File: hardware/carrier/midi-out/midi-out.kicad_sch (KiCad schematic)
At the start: 7 parts

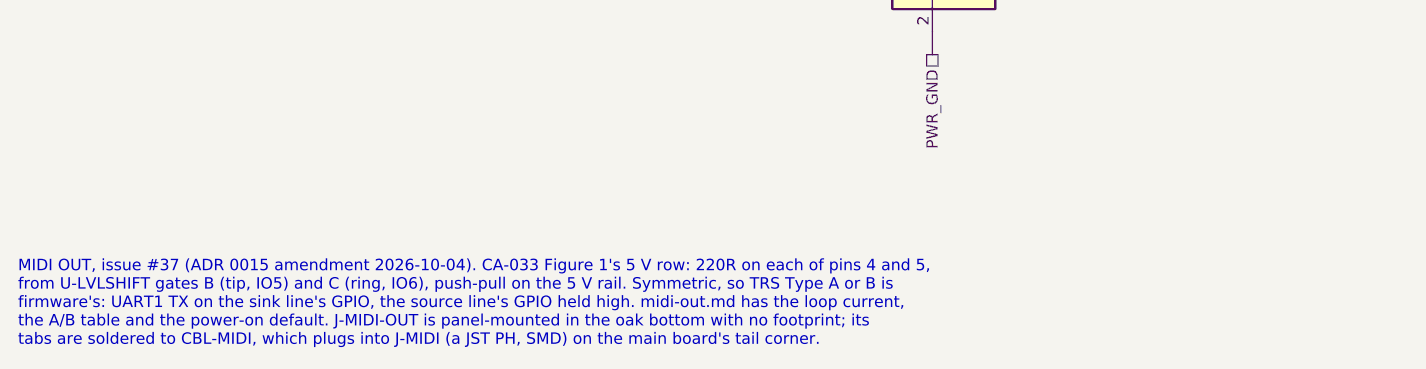
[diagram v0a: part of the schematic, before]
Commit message: #37: midi-out sheet text named the old GPIOs; carrier sheet renders re-ledgered
The midi-out sheet's note said gates B (tip, IO5) and C (ring, IO6).
It is IO6 and IO2 since the ribbon re-pin. Fixed and re-rendered. The
carrier, led-strip-drive, breath-adc and power-entry-instrument renders came
out identical and are re-ledgered in hardware/SHEETS.csv.

Gate-Red: pre-existing main-board/module-main kicad failures; boards/module-iso has no coverage row (arrived with integration bcd1f0c); interfaces/system sim stale; body renders and photos deferred to one rebuild after #36/#37 merge (coordinator); DXFs and clash pending (one heavy job at a time); main-board.kicad_pcb parity on IO2/IO6 and U-LVLSHIFT pins 5/6/8/9, R48/R49 and the MIDI parts unplaced (#35 has the board)

Co-Authored-By: Claude Opus 5.5 <noreply@anthropic.com>
Claude-Session: https://claude.ai/code/session_01LmB4muFXnoLprWX4JzuJ5A
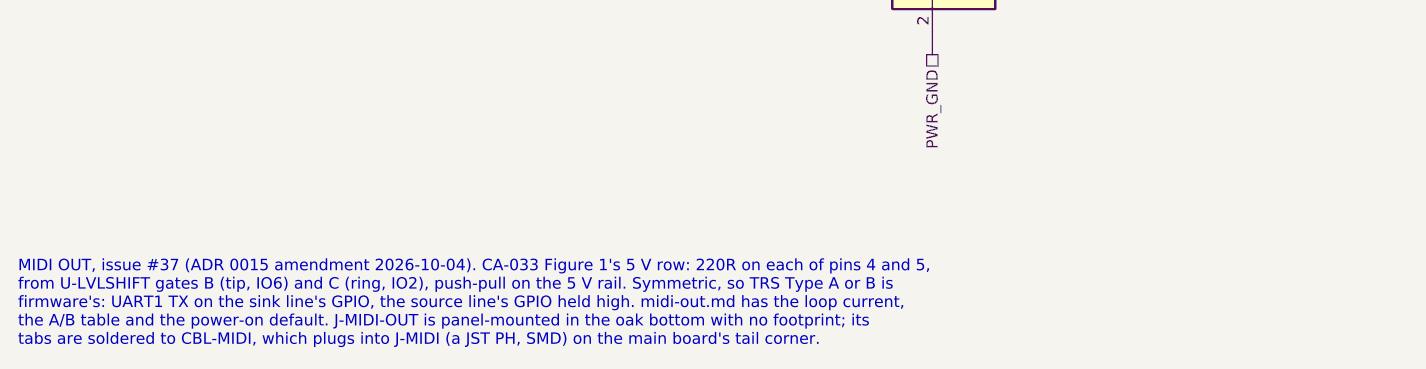
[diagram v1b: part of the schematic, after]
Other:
- note added: "MIDI OUT, issue #37 (ADR 0015 amendment 2026-10-04). CA-033 Figure 1's 5 V row: 220R on each of pins 4 and 5, from U-LVLSHIFT gates B (tip, IO6) and C (ring, IO2), push-pull on the 5 V rail. Symmetric, so TRS Type A or B is firmware's: UART1 TX on the sink line's GPIO, the source line's GPIO held high. midi-out.md has the loop current, the A/B table and the power-on default. J-MIDI-OUT is panel-m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"
- note removed: "MIDI OUT, issue #37 (ADR 0015 amendment 2026-10-04). CA-033 Figure 1's 5 V row: 220R on each of pins 4 and 5, from U-LVLSHIFT gates B (tip, IO5) and C (ring, IO6), push-pull on the 5 V rail. Symmetric, so TRS Type A or B is firmware's: UART1 TX on the sink line's GPIO, the source line's GPIO held high. midi-out.md has the loop current, the A/B table and the power-on default. J-MIDI-OUT is panel-m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"
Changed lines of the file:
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@@
     (property "From" "module/power-entry" (at 220.98 66.04 0) (effects (font (size 1.27 1.27)) hide))
     (property "Figure" "dig-gnd-topology" (at 220.98 66.04 0) (effects (font (size 1.27 1.27)) hide)))
-  (text "MIDI OUT, issue #37 (ADR 0015 amendment 2026-10-04). CA-033 Figure 1's 5 V row: 220R on each of pins 4 and 5,\nfrom U-LVLSHIFT gates B (tip, IO5) and C (ring, IO6), push-pull on the 5 V rail. Symmetric, so TRS Type A or B is\nfirmware's: UART1 TX on the sink line's GPIO, the source line's GPIO held high. midi-out.md has the loop current,\nthe A/B table and the power-on default. J-MIDI-OUT is panel-mounted in the oak bottom with no footprint; its\ntabs are soldered to CBL-MIDI, which plugs into J-MIDI (a JST PH, SMD) on the main board's tail corner." (at 20.32 137.16 0) (effects (font (size 1.27 1.27)) (justify left top)))
+  (text "MIDI OUT, issue #37 (ADR 0015 amendment 2026-10-04). CA-033 Figure 1's 5 V row: 220R on each of pins 4 and 5,\nfrom U-LVLSHIFT gates B (tip, IO6) and C (ring, IO2), push-pull on the 5 V rail. Symmetric, so TRS Type A or B is\nfirmware's: UART1 TX on the sink line's GPIO, the source line's GPIO held high. midi-out.md has the loop current,\nthe A/B table and the power-on default. J-MIDI-OUT is panel-mounted in the oak bottom with no footprint; its\ntabs are soldered to CBL-MIDI, which plugs into J-MIDI (a JST PH, SMD) on the main board's tail corner." (at 20.32 137.16 0) (effects (font (size 1.27 1.27)) (justify left top)))
   (sheet_instances (path "/" (page "1")))
 )

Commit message: #39: ideal-diode 5 V OR (U-USBOR LM74700-Q1 + Q-USBOR DMN3404L) replaces D-USBOR; R-MIDI 182R 1%
Checkpoint. D-USBOR's SS14 is replaced on power-entry-instrument by an
LM74700-Q1 ideal-diode controller and a DMN3404L N-FET (C-USBOR x2 for its
VCAP and CATHODE), datasheets banked (.manifest-R56). INST_5V_A with the
rack up is 4.625-5.325 V (sim or-rack); no back-feed either way (or-both),
switch-over and rack-loss simulated. R-MIDI-T/R are 182R 1% (UNI-ROYAL
1206W4F1820T5E, C247358), sized to the gate's 25 mA at the rail's ceiling.
MIDI worst corner 3.69 mA: still under CA-033's 3.75 mA, kept recorded.

Gate-Red: main-board parity (main-board.kicad_pcb deliberately not touched: D4 gone, U13/Q2/C207/C208 unplaced, fab/ stale - another agent places them); midi-out and main-board renders not yet regenerated for R-MIDI's value (next commit); interfaces/system sim stale (pre-existing, re-run in progress); 38 stale CAD renders and module-iso coverage (pre-existing; no bulk CAD renders allowed)

Co-Authored-By: Claude Opus 5.5 <noreply@anthropic.com>
Claude-Session: https://claude.ai/code/session_01LmB4muFXnoLprWX4JzuJ5A
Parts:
- R-MIDI-R: value 220R -> 182R 1%; LCSC (none) -> C247358; MPN 1206W4J0221T5E -> 1206W4F1820T5E
- R-MIDI-T: value 220R -> 182R 1%; LCSC (none) -> C247358; MPN 1206W4J0221T5E -> 1206W4F1820T5E; Note TIP's series resistor, CA-033 Figure 1's 5 V row (220 ohm 5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 -> TIP's series resistor: CA-033 Figure 1's 5 V row, re-sized 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
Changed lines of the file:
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@@
     (in_bom yes) (on_board yes) (dnp no)
     (property "Reference" "R-MIDI-T" (at 60.96 48.26 90) (effects (font (size 1.27 1.27))))
-    (property "Value" "220R" (at 60.96 53.34 90) (effects (font (size 1.27 1.27))))
+    (property "Value" "182R 1%" (at 60.96 53.34 90) (effects (font (size 1.27 1.27))))
     (property "Footprint" "Resistor_SMD:R_1206_3216Metric" (at 60.96 52.07 0) (effects (font (size 1.27 1.27)) hide))
     (property "Datasheet" "" (at 60.96 50.8 0) (effects (font (size 1.27 1.27)) hide))
     (property "Row" "R-MIDI" (at 60.96 50.8 0) (effects (font (size 1.27 1.27)) hide))
     (property "Pins" "1=1 2=2" (at 60.96 50.8 0) (effects (font (size 1.27 1.27)) hide))
-    (property "Note" "TIP's series resistor, CA-033 Figure 1's 5 V row (220 ohm 5 % 0.25 W) [ds connectors/MIDI-CA-033-ELECTRICAL-SPEC-UPDATE-2014.pdf p.3]. It is RA when the tip is the source (Type B) and RC when it is the sink (Type A): the two lines are identical so the choice is firmware's. Limits a short of the tip to the sleeve to 5.0 V / 209 ohm = 23.9 mA, inside U-LVLSHIFT's 25 mA continuous rating (midi-out.md)" (at 60.96 50.8 0) (effects (font (size 1.27 1.27)) hide))
+    (property "Note" "TIP's series resistor: CA-033 Figure 1's 5 V row, re-sized to 182 ohm 1 % 0.25 W (issue #39) - the smallest E96 value that holds a short of the tip to the sleeve under U-LVLSHIFT's 25 mA absolute maximum at the rail's ceiling, the resistor at -1 % (midi-out.md, Why not lower resistors). DO NOT FIT 5 %: the derivation needs 1 %. It is RA when the tip is the source (Type B) and RC when it is the sink (Type A): the two lines are identical so the choice is firmware's" (at 60.96 50.8 0) (effects (font (size 1.27 1.27)) hide))
     (pin "1")
     (pin "2")
     (property "Manufacturer" "UNI-ROYAL" (at 60.96 50.8 0) (effects (font (size 1.27 1.27)) hide))
-    (property "MPN" "1206W4J0221T5E" (at 60.96 50.8 0) (effects (font (size 1.27 1.27)) hide))
-    (property "LCSC" "" (at 60.96 50.8 0) (effects (font (size 1.27 1.27)) hide))
+    (property "MPN" "1206W4F1820T5E" (at 60.96 50.8 0) (effects (font (size 1.27 1.27)) hide))
+    (property "LCSC" "C247358" (at 60.96 50.8 0) (effects (font (size 1.27 1.27)) hide))
     (property "Assembly" "machine" (at 60.96 50.8 0) (effects (font (size 1.27 1.27)) hide))
     (property "Pins_source" "a two-terminal resistor" (at 60.96 50.8 0) (effects (font (size 1.27 1.27)) hide))
@@
     (in_bom yes) (on_board yes) (dnp no)
     (property "Reference" "R-MIDI-R" (at 60.96 73.66 90) (effects (font (size 1.27 1.27))))
-    (property "Value" "220R" (at 60.96 78.74 90) (effects (font (size 1.27 1.27))))
+    (property "Value" "182R 1%" (at 60.96 78.74 90) (effects (font (size 1.27 1.27))))
     (property "Footprint" "Resistor_SMD:R_1206_3216Metric" (at 60.96 77.47 0) (effects (font (size 1.27 1.27)) hide))
     (property "Datasheet" "" (at 60.96 76.2 0) (effects (font (size 1.27 1.27)) hide))
@@
     (pin "2")
     (property "Manufacturer" "UNI-ROYAL" (at 60.96 76.2 0) (effects (font (size 1.27 1.27)) hide))
-    (property "MPN" "1206W4J0221T5E" (at 60.96 76.2 0) (effects (font (size 1.27 1.27)) hide))
-    (property "LCSC" "" (at 60.96 76.2 0) (effects (font (size 1.27 1.27)) hide))
+    (property "MPN" "1206W4F1820T5E" (at 60.96 76.2 0) (effects (font (size 1.27 1.27)) hide))
+    (property "LCSC" "C247358" (at 60.96 76.2 0) (effects (font (size 1.27 1.27)) hide))
     (property "Assembly" "machine" (at 60.96 76.2 0) (effects (font (size 1.27 1.27)) hide))
     (property "Pins_source" "a two-terminal resistor" (at 60.96 76.2 0) (effects (font (size 1.27 1.27)) hide))

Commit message: #45 parts and docs: J-MIDI side entry (S3B-PH-SM4-TB), J-MIDI-OUT in the tail cap, ADR 0021 amended
- midi-out.kicad_sch: J-MIDI is the side-entry S3B-PH-SM4-TB(LF)(SN), LCSC
  C265101, on woody:JST_PH_S3B-PH-SM4-TB_1x03-1MP_P2.00mm_Horizontal (still
  Assembly hand); J-MIDI-OUT's note puts it through the tail cap. netlist.yaml
  and the sheet render re-exported; the sim re-run (0 failed).
- hardware/lib/woody.pretty: KiCad 9's S3B footprint, banked with the
  banked EasyEDA/LCSC STEP for C265101 at (2, -2.9, 0), so the model survives
  a footprint refresh.
- datasheets: the STEP and the EasyEDA footprint JSON (JLC's is KiCad's
  turned 180 degrees), and LCSC's datasheet URL as BLOCKED, in
  .manifest-R59-j7-side-entry.csv; MANIFEST.csv merged.
- BOM fragments: J-MIDI, J-MIDI-OUT, CBL-MIDI; ENDCAP-TAIL's note loses the
  USB-C slot issue #37 removed and gains the jack. bom.csv merged.
- midi-out.md (and a new notes.md for the oak-bottom design), lib README,
  README, ROADMAP, firmware README.
- ADR 0021, Amendment, 2026-10-07, with both owner quotes. It records that
  the first fit study's "does not fit" was wrong (the jack's drawing misread,
  and the jack's cut kept apart from the etherCON's recess), and that the
  corner is the owner's choice.

check-netlist --strict: 0 problems. merge-bom --check: 0 problems.
verify-datasheets: 0 problems.

Gate-Red: main-board.kicad_pcb and its layout.yaml still place the top-entry J7 and the off-centre J-UMB (the board half of #45 follows separately); body renders/photos/clash and unaffected DXFs left for the render pass; inherited module clash, module-iso sim coverage, photo-hero ledger

Co-Authored-By: Claude Opus 5.5 <noreply@anthropic.com>
Claude-Session: https://claude.ai/code/session_01LmB4muFXnoLprWX4JzuJ5A
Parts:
- J-MIDI: value B3B-PH-SM4-TB -> S3B-PH-SM4-TB; footprint Connector_JST:JST_PH_B3B-PH-SM4-TB_1x03-1MP_P2.00mm_Vertical -> woody:JST_PH_S3B-PH-SM4-TB_1x03-1MP_P2.00mm_Horizontal; LCSC (none) -> C265101; MPN B3B-PH-SM4-TB(LF)(SN) -> S3B-PH-SM4-TB(LF)(SN); Note The MIDI jack's lead plugs in here, on the main board's fre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 -> The MIDI jack's lead plugs in here (issue #45): pin 1 MIDI_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; Pins_source JST PH, surface mount, top entry: pin 1 by the shroud's key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 -> JST PH, surface mount, side entry: pin 1 at the end the dra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
- J-MIDI-OUT: Note PANEL-MOUNTED THROUGH THE OAK BOTTOM, NO FOOTPRINT (owner, 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 -> PANEL-MOUNTED THROUGH THE TAIL CAP, NO FOOTPRINT (owner, 20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
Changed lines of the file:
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@@
     (in_bom yes) (on_board yes) (dnp no)
     (property "Reference" "J-MIDI" (at 167.64 55.88 0) (effects (font (size 1.27 1.27))))
-    (property "Value" "B3B-PH-SM4-TB" (at 167.64 58.42 0) (effects (font (size 1.27 1.27))))
-    (property "Footprint" "Connector_JST:JST_PH_B3B-PH-SM4-TB_1x03-1MP_P2.00mm_Vertical" (at 167.64 63.5 0) (effects (font (size 1.27 1.27)) hide))
+    (property "Value" "S3B-PH-SM4-TB" (at 167.64 58.42 0) (effects (font (size 1.27 1.27))))
+    (property "Footprint" "woody:JST_PH_S3B-PH-SM4-TB_1x03-1MP_P2.00mm_Horizontal" (at 167.64 63.5 0) (effects (font (size 1.27 1.27)) hide))
     (property "Datasheet" "" (at 167.64 63.5 0) (effects (font (size 1.27 1.27)) hide))
     (property "Row" "J-MIDI" (at 167.64 63.5 0) (effects (font (size 1.27 1.27)) hide))
     (property "Pins" "1=1 2=2 3=3" (at 167.64 63.5 0) (effects (font (size 1.27 1.27)) hide))
-    (property "Note" "The MIDI jack's lead plugs in here, on the main board's freed tail corner (issue #37): pin 1 MIDI_TIP, pin 2 MIDI_RING, pin 3 PWR_GND. A JST PH, surface mount and top entry, so no tails stand under the board over the bottom plate. Polarised; reached with the lid off after the cassette drops in, as HDR-SERVICE is" (at 167.64 63.5 0) (effects (font (size 1.27 1.27)) hide))
+    (property "Note" "The MIDI jack's lead plugs in here (issue #45): pin 1 MIDI_TIP, pin 2 MIDI_RING, pin 3 PWR_GND. A JST PH, surface mount and SIDE entry, its mouth facing the tail (owner, 2026-10-07: 'a 90deg facing the rear'), so the lead runs straight back to the jack in the tail cap and no tails stand under the board over the bottom plate. Polarised; reached with the lid off after the cassette drops in, as HDR-SERVICE is" (at 167.64 63.5 0) (effects (font (size 1.27 1.27)) hide))
     (pin "1")
     (pin "2")
     (pin "3")
     (property "Manufacturer" "JST" (at 167.64 63.5 0) (effects (font (size 1.27 1.27)) hide))
-    (property "MPN" "B3B-PH-SM4-TB(LF)(SN)" (at 167.64 63.5 0) (effects (font (size 1.27 1.27)) hide))
-    (property "LCSC" "" (at 167.64 63.5 0) (effects (font (size 1.27 1.27)) hide))
+    (property "MPN" "S3B-PH-SM4-TB(LF)(SN)" (at 167.64 63.5 0) (effects (font (size 1.27 1.27)) hide))
+    (property "LCSC" "C265101" (at 167.64 63.5 0) (effects (font (size 1.27 1.27)) hide))
     (property "Assembly" "hand" (at 167.64 63.5 0) (effects (font (size 1.27 1.27)) hide))
-    (property "Pins_source" "JST PH, surface mount, top entry: pin 1 by the shroud's key [from memory; JST's drawing to bank with the part]" (at 167.64 63.5 0) (effects (font (size 1.27 1.27)) hide))
+    (property "Pins_source" "JST PH, surface mount, side entry: pin 1 at the end the drawing's 'Mark of No. 1 circuit' marks [ds datasheets/connectors/JST-PH-SERIES.pdf p.4, Header (SMT type), side entry]; JLC's library footprint for C265101 numbers them the same way, turned 180 degrees [ds datasheets/connectors/EASYEDA-C265101-S3B-PH-SM4-TB-FOOTPRINT.json]" (at 167.64 63.5 0) (effects (font (size 1.27 1.27)) hide))
     (instances (project "main-board" (path "/b12a49ac-ffa0-5078-b2ba-e15d161f1936/e02c6272-2aa9-4bec-ba9c-1e4212a18689" (reference "J7") (unit 1))) (project "midi-out" (path "/4b60816b-23dc-5f77-b39b-2d8620b1398e" (reference "J-MIDI") (unit 1))))
   )
@@
     (property "Row" "J-MIDI-OUT" (at 228.6 63.5 0) (effects (font (size 1.27 1.27)) hide))
     (property "Pins" "T=T R1=R1 R2=R2 S=S" (at 228.6 63.5 0) (effects (font (size 1.27 1.27)) hide))
-    (property "Note" "PANEL-MOUNTED THROUGH THE OAK BOTTOM, NO FOOTPRINT (owner, 2026-10-04: \"on the bottom face, and then just do a connector to the main board\"): its tabs are soldered to CBL-MIDI, which plugs into J-MIDI. A 4-conductor jack taking a 3-conductor plug: the plug's sleeve spans R2 and S, so both are PWR_GND (MIDI pin 2, grounded at the transmitter only) [ds connectors/SAMESKY-SJ5-43502PM.pdf p.2]" (at 228.6 63.5 0) (effects (font (size 1.27 1.27)) hide))
+    (property "Note" "PANEL-MOUNTED THROUGH THE TAIL CAP, NO FOOTPRINT (owner, 2026-10-07: \"TRS connector should be on the same side as the ethercon on the controller\"; issue #45): in a corner of the tail face beside the etherCON, its tabs are soldered to CBL-MIDI, which plugs into J-MIDI. A 4-conductor jack taking a 3-conductor plug: the plug's sleeve spans R2 and S, so both are PWR_GND (MIDI pin 2, grounded at the transmitter only) [ds connectors/SAMESKY-SJ5-43502PM.pdf p.2]" (at 228.6 63.5 0) (effects (font (size 1.27 1.27)) hide))
     (property "Pins_source" "datasheets/connectors/SAMESKY-SJ5-43502PM.pdf p.2: 1 tip, 2 ring 1, 3 ring 2, 4 sleeve (KiCad's AudioJack4 names them T, R1, R2, S)" (at 228.6 63.5 0) (effects (font (size 1.27 1.27)) hide))
     (pin "R1")
